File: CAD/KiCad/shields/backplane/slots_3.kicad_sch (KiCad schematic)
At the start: 2 parts

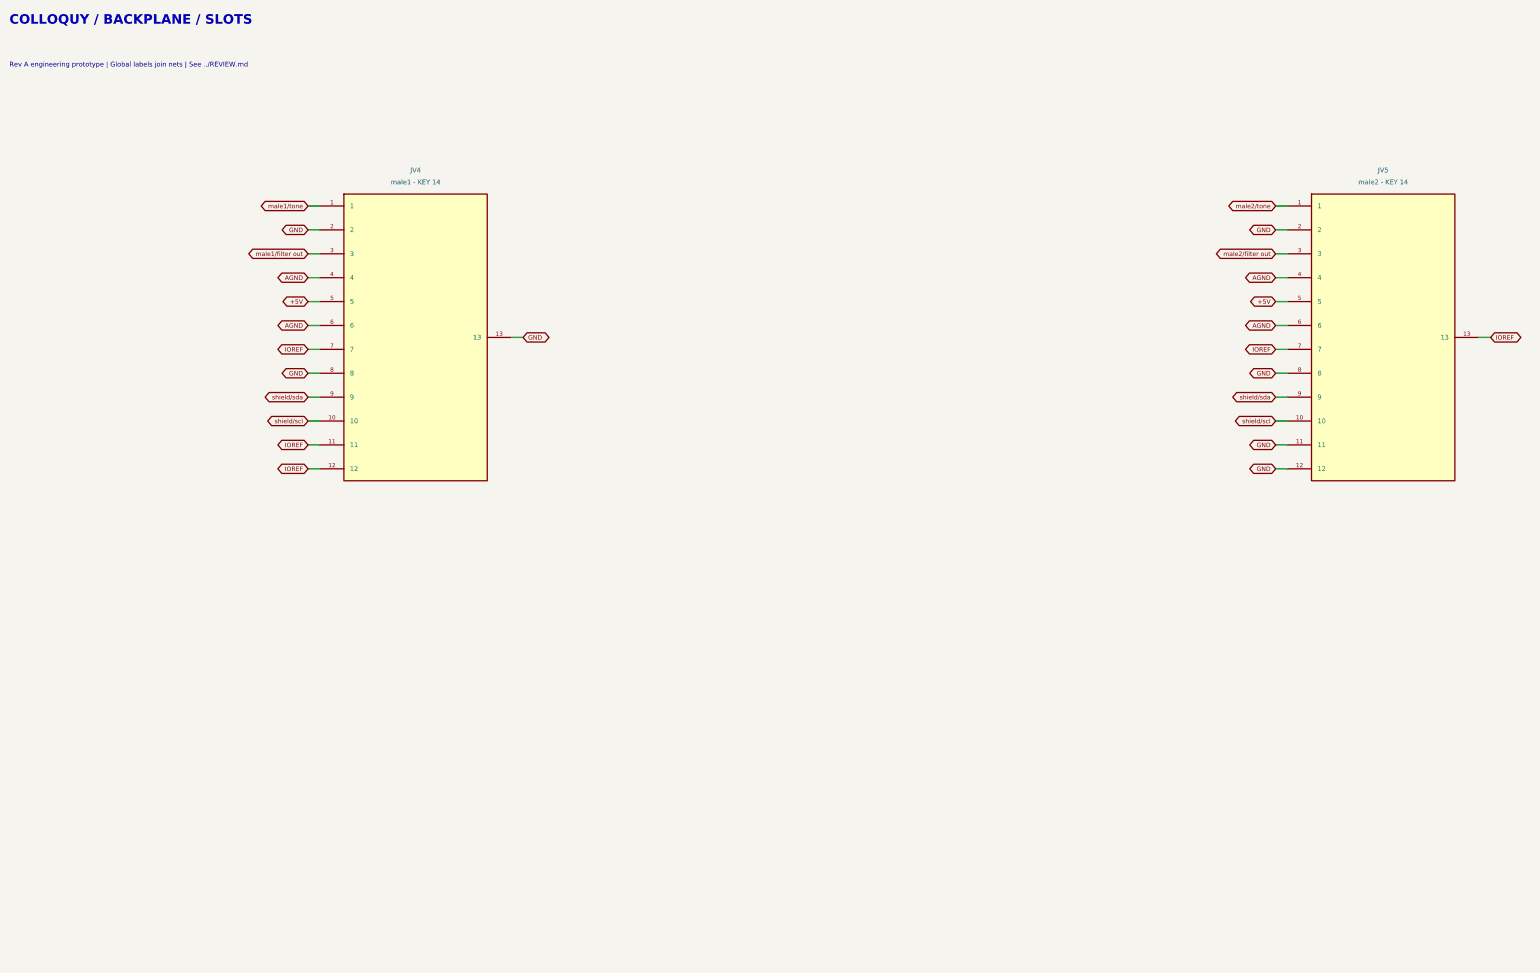
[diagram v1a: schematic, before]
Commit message: Remove shield identification and adopt the simplified connector and Teensy pin maps
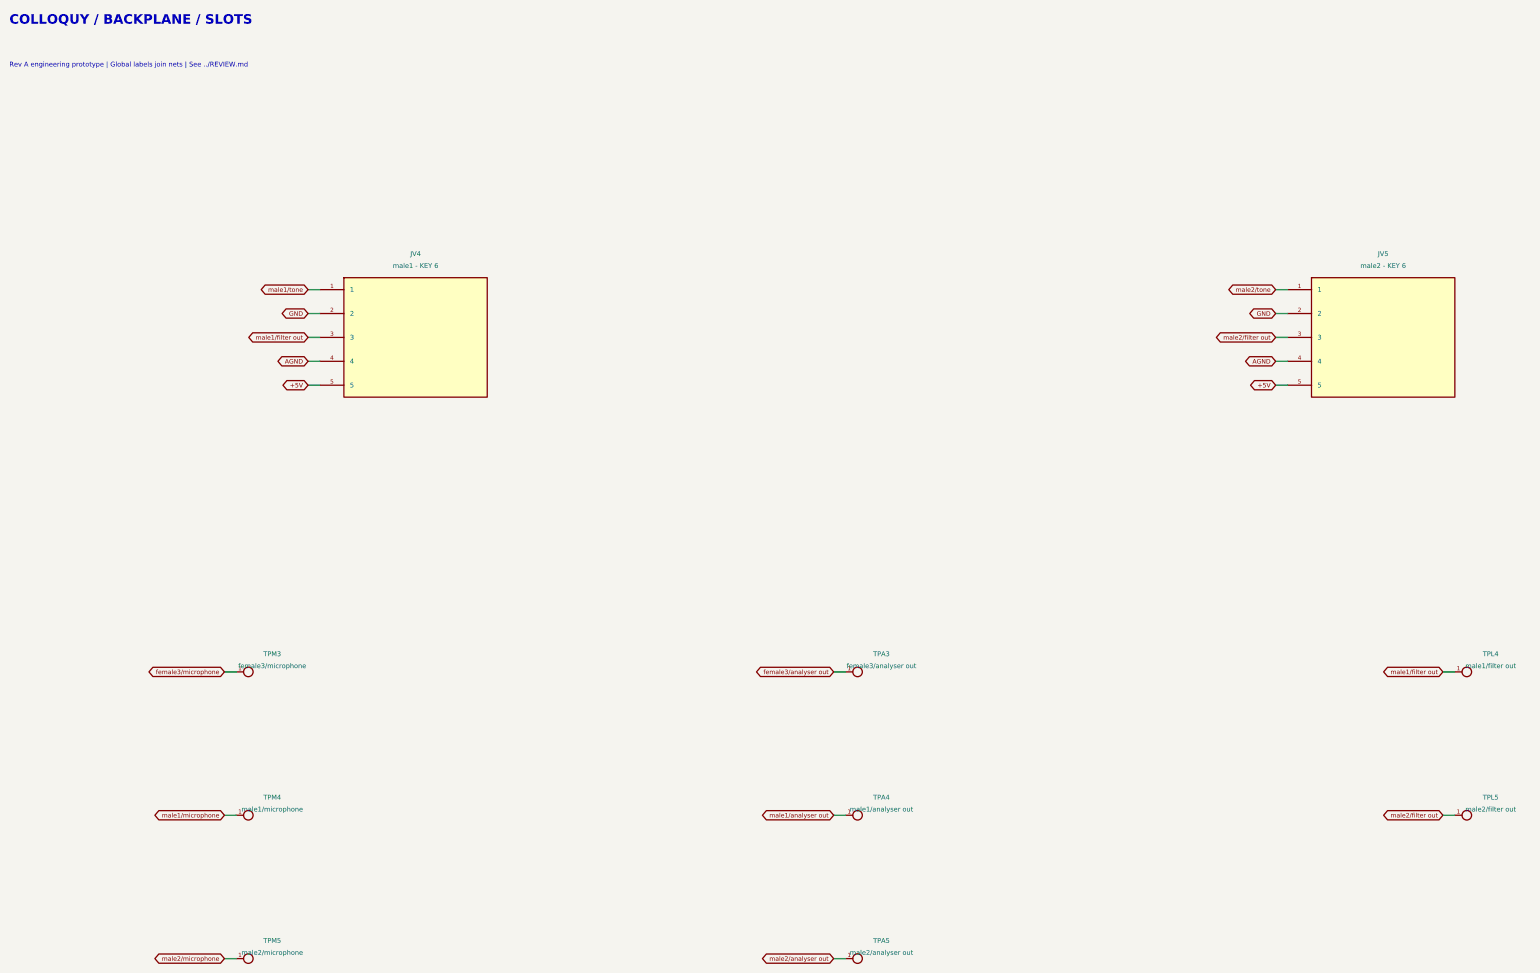
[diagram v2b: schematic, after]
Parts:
- added TPA3: female3/analyser out, Shields:TestPoint_Pad_D1.5mm, symbol Colloquy:TPA3
- added TPA4: male1/analyser out, Shields:TestPoint_Pad_D1.5mm, symbol Colloquy:TPA4
- added TPA5: male2/analyser out, Shields:TestPoint_Pad_D1.5mm, symbol Colloquy:TPA5
- added TPL4: male1/filter out, Shields:TestPoint_Pad_D1.5mm, symbol Colloquy:TPL4
- added TPL5: male2/filter out, Shields:TestPoint_Pad_D1.5mm, symbol Colloquy:TPL5
- added TPM3: female3/microphone, Shields:TestPoint_Pad_D1.5mm, symbol Colloquy:TPM3
- added TPM4: male1/microphone, Shields:TestPoint_Pad_D1.5mm, symbol Colloquy:TPM4
- added TPM5: male2/microphone, Shields:TestPoint_Pad_D1.5mm, symbol Colloquy:TPM5
- JV4: value male1 - KEY 14 -> male1 - KEY 6; footprint Shields:Header_2x07_Key14 -> Shields:Header_2x03_Key6
- JV5: value male2 - KEY 14 -> male2 - KEY 6; footprint Shields:Header_2x07_Key14 -> Shields:Header_2x03_Key6
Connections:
- net AGND: no longer JV4.6, JV5.6
- net GND: no longer JV4.13, JV4.8, JV5.11, JV5.12, JV5.8
- net male1/filter out: now also TPL4.1
- net male2/filter out: now also TPL5.1
- removed net IOREF: JV4.11, JV4.12, JV4.7, JV5.13, JV5.7
- removed net shield/scl: JV4.10, JV5.10
- removed net shield/sda: JV4.9, JV5.9
- new net female3/analyser out: TPA3.1
- new net female3/microphone: TPM3.1
- new net male1/analyser out: TPA4.1
- new net male1/microphone: TPM4.1
- new net male2/analyser out: TPA5.1
- new net male2/microphone: TPM5.1

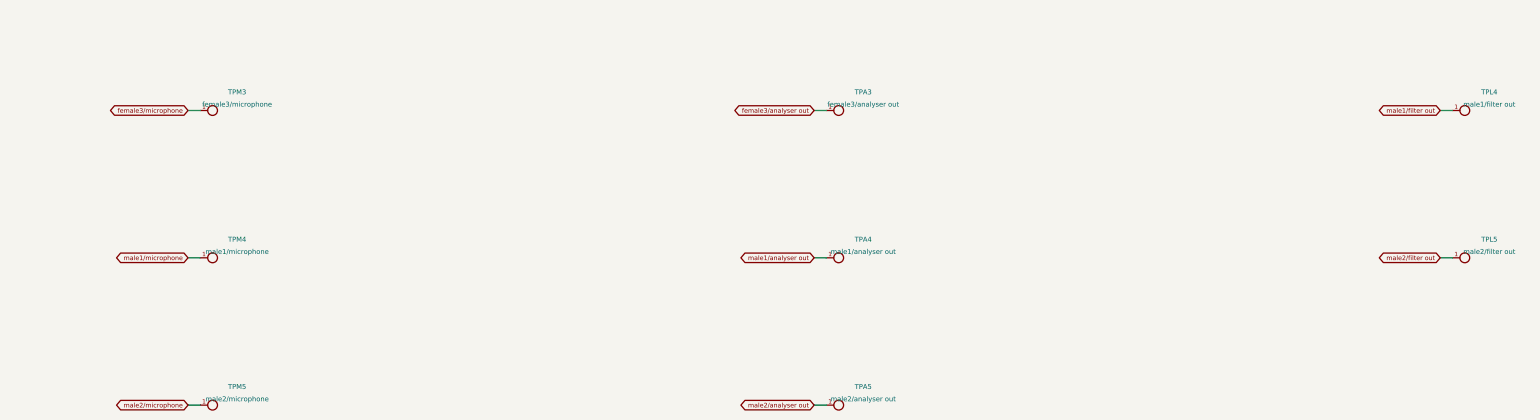
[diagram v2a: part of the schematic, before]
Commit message: Route microphones directly to Teensy and remove the analyser buffer board
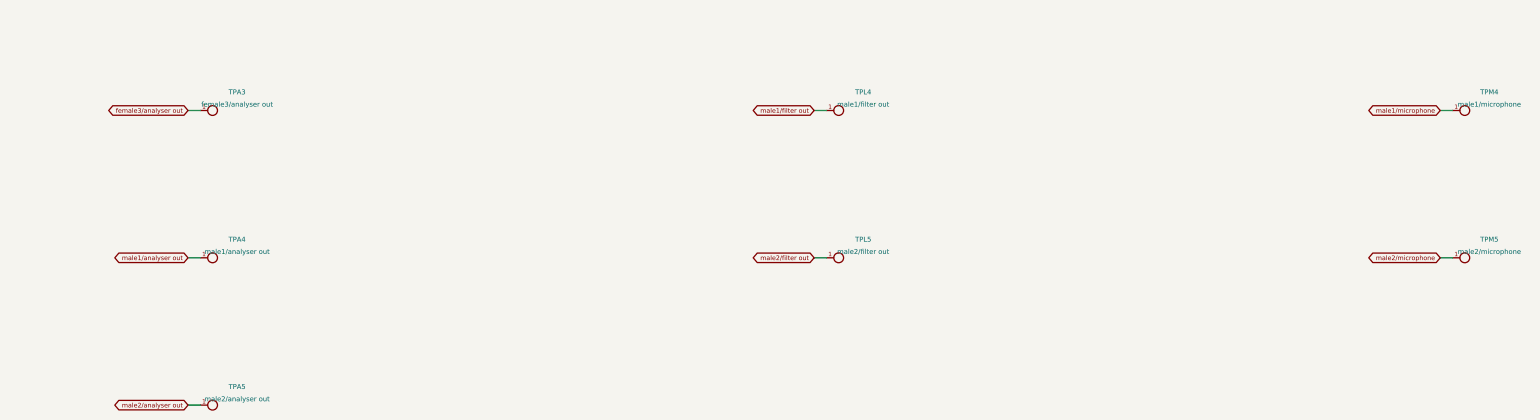
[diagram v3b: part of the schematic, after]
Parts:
- removed TPM3: female3/microphone, Shields:TestPoint_Pad_D1.5mm, symbol Colloquy:TPM3
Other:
- moved on the sheet: TPA3, TPA4, TPA5, TPL4, TPL5, TPM4, TPM5

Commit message: Update shields for Thomas RC cards, debug headers and body microphones
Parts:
- removed TPA3: female3/analyser out, Shields:TestPoint_Pad_D1.5mm, symbol Colloquy:TPA3
- removed TPA4: male1/analyser out, Shields:TestPoint_Pad_D1.5mm, symbol Colloquy:TPA4
- removed TPA5: male2/analyser out, Shields:TestPoint_Pad_D1.5mm, symbol Colloquy:TPA5
- removed TPL4: male1/filter out, Shields:TestPoint_Pad_D1.5mm, symbol Colloquy:TPL4
- removed TPL5: male2/filter out, Shields:TestPoint_Pad_D1.5mm, symbol Colloquy:TPL5
- removed TPM4: male1/microphone, Shields:TestPoint_Pad_D1.5mm, symbol Colloquy:TPM4
- removed TPM5: male2/microphone, Shields:TestPoint_Pad_D1.5mm, symbol Colloquy:TPM5
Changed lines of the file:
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@@
 (wire (pts (xy 287.0200 93.9800) (xy 284.4800 93.9800)) (stroke (width 0) (type default)))
 (global_label "+5V" (shape bidirectional) (at 284.4800 93.9800 180) (effects (font (size 0.95 0.95)) (justify right)) (property "Intersheetrefs" "${INTERSHEET_REFS}" (at 284.4800 93.9800 0) (effects (font (size 1.016 1.016))  (hide yes))))
-(symbol (lib_id "Colloquy:TPA3") (at 66.0400 154.9400 0) (unit 1) (exclude_from_sim no) (in_bom no) (on_board yes) (dnp no)
-(property "Reference" "TPA3" (at 71.1200 151.1300 0) (effects (font (size 1.016 1.016))  ))
-(property "Value" "female3/analyser out" (at 71.1200 153.6700 0) (effects (font (size 1.016 1.016))  ))
-(property "Footprint" "Shields:TestPoint_Pad_D1.5mm" (at 66.0400 154.9400 0) (effects (font (size 1.27 1.27))  (hide yes)))
-(property "Datasheet" "" (at 66.0400 154.9400 0) (effects (font (size 1.27 1.27))  (hide yes)))
-(property "Description" "" (at 66.0400 154.9400 0) (effects (font (size 1.27 1.27))  (hide yes)))
-(pin "1")
-(instances (project "backplane" (path "/c974ff16-a701-53ef-8165-966482bbbbae/41ae4712-1962-5c99-85ef-a0ccc72ad0b9" (reference "TPA3") (unit 1)))))
-(wire (pts (xy 63.5000 154.9400) (xy 60.9600 154.9400)) (stroke (width 0) (type default)))
-(global_label "female3/analyser out" (shape bidirectional) (at 60.9600 154.9400 180) (effects (font (size 0.95 0.95)) (justify right)) (property "Intersheetrefs" "${INTERSHEET_REFS}" (at 60.9600 154.9400 0) (effects (font (size 1.016 1.016))  (hide yes))))
-(symbol (lib_id "Colloquy:TPL4") (at 195.5800 154.9400 0) (unit 1) (exclude_from_sim no) (in_bom no) (on_board yes) (dnp no)
-(property "Reference" "TPL4" (at 200.6600 151.1300 0) (effects (font (size 1.016 1.016))  ))
-(property "Value" "male1/filter out" (at 200.6600 153.6700 0) (effects (font (size 1.016 1.016))  ))
-(property "Footprint" "Shields:TestPoint_Pad_D1.5mm" (at 195.5800 154.9400 0) (effects (font (size 1.27 1.27))  (hide yes)))
-(property "Datasheet" "" (at 195.5800 154.9400 0) (effects (font (size 1.27 1.27))  (hide yes)))
-(property "Description" "" (at 195.5800 154.9400 0) (effects (font (size 1.27 1.27))  (hide yes)))
-(pin "1")
-(instances (project "backplane" (path "/c974ff16-a701-53ef-8165-966482bbbbae/41ae4712-1962-5c99-85ef-a0ccc72ad0b9" (reference "TPL4") (unit 1)))))
-(wire (pts (xy 193.0400 154.9400) (xy 190.5000 154.9400)) (stroke (width 0) (type default)))
-(global_label "male1/filter out" (shape bidirectional) (at 190.5000 154.9400 180) (effects (font (size 0.95 0.95)) (justify right)) (property "Intersheetrefs" "${INTERSHEET_REFS}" (at 190.5000 154.9400 0) (effects (font (size 1.016 1.016))  (hide yes))))
-(symbol (lib_id "Colloquy:TPM4") (at 325.1200 154.9400 0) (unit 1) (exclude_from_sim no) (in_bom no) (on_board yes) (dnp no)
-(property "Reference" "TPM4" (at 330.2000 151.1300 0) (effects (font (size 1.016 1.016))  ))
-(property "Value" "male1/microphone" (at 330.2000 153.6700 0) (effects (font (size 1.016 1.016))  ))
-(property "Footprint" "Shields:TestPoint_Pad_D1.5mm" (at 325.1200 154.9400 0) (effects (font (size 1.27 1.27))  (hide yes)))
-(property "Datasheet" "" (at 325.1200 154.9400 0) (effects (font (size 1.27 1.27))  (hide yes)))
-(property "Description" "" (at 325.1200 154.9400 0) (effects (font (size 1.27 1.27))  (hide yes)))
-(pin "1")
-(instances (project "backplane" (path "/c974ff16-a701-53ef-8165-966482bbbbae/41ae4712-1962-5c99-85ef-a0ccc72ad0b9" (reference "TPM4") (unit 1)))))
-(wire (pts (xy 322.5800 154.9400) (xy 320.0400 154.9400)) (stroke (width 0) (type default)))
-(global_label "male1/microphone" (shape bidirectional) (at 320.0400 154.9400 180) (effects (font (size 0.95 0.95)) (justify right)) (property "Intersheetrefs" "${INTERSHEET_REFS}" (at 320.0400 154.9400 0) (effects (font (size 1.016 1.016))  (hide yes))))
-(symbol (lib_id "Colloquy:TPA4") (at 66.0400 185.4200 0) (unit 1) (exclude_from_sim no) (in_bom no) (on_board yes) (dnp no)
-(property "Reference" "TPA4" (at 71.1200 181.6100 0) (effects (font (size 1.016 1.016))  ))
-(property "Value" "male1/analyser out" (at 71.1200 184.1500 0) (effects (font (size 1.016 1.016))  ))
-(property "Footprint" "Shields:TestPoint_Pad_D1.5mm" (at 66.0400 185.4200 0) (effects (font (size 1.27 1.27))  (hide yes)))
-(property "Datasheet" "" (at 66.0400 185.4200 0) (effects (font (size 1.27 1.27))  (hide yes)))
-(property "Description" "" (at 66.0400 185.4200 0) (effects (font (size 1.27 1.27))  (hide yes)))
-(pin "1")
-(instances (project "backplane" (path "/c974ff16-a701-53ef-8165-966482bbbbae/41ae4712-1962-5c99-85ef-a0ccc72ad0b9" (reference "TPA4") (unit 1)))))
-(wire (pts (xy 63.5000 185.4200) (xy 60.9600 185.4200)) (stroke (width 0) (type default)))
-(global_label "male1/analyser out" (shape bidirectional) (at 60.9600 185.4200 180) (effects (font (size 0.95 0.95)) (justify right)) (property "Intersheetrefs" "${INTERSHEET_REFS}" (at 60.9600 185.4200 0) (effects (font (size 1.016 1.016))  (hide yes))))
-(symbol (lib_id "Colloquy:TPL5") (at 195.5800 185.4200 0) (unit 1) (exclude_from_sim no) (in_bom no) (on_board yes) (dnp no)
-(property "Reference" "TPL5" (at 200.6600 181.6100 0) (effects (font (size 1.016 1.016))  ))
-(property "Value" "male2/filter out" (at 200.6600 184.1500 0) (effects (font (size 1.016 1.016))  ))
-(property "Footprint" "Shields:TestPoint_Pad_D1.5mm" (at 195.5800 185.4200 0) (effects (font (size 1.27 1.27))  (hide yes)))
-(property "Datasheet" "" (at 195.5800 185.4200 0) (effects (font (size 1.27 1.27))  (hide yes)))
-(property "Description" "" (at 195.5800 185.4200 0) (effects (font (size 1.27 1.27))  (hide yes)))
-(pin "1")
-(instances (project "backplane" (path "/c974ff16-a701-53ef-8165-966482bbbbae/41ae4712-1962-5c99-85ef-a0ccc72ad0b9" (reference "TPL5") (unit 1)))))
-(wire (pts (xy 193.0400 185.4200) (xy 190.5000 185.4200)) (stroke (width 0) (type default)))
-(global_label "male2/filter out" (shape bidirectional) (at 190.5000 185.4200 180) (effects (font (size 0.95 0.95)) (justify right)) (property "Intersheetrefs" "${INTERSHEET_REFS}" (at 190.5000 185.4200 0) (effects (font (size 1.016 1.016))  (hide yes))))
-(symbol (lib_id "Colloquy:TPM5") (at 325.1200 185.4200 0) (unit 1) (exclude_from_sim no) (in_bom no) (on_board yes) (dnp no)
-(property "Reference" "TPM5" (at 330.2000 181.6100 0) (effects (font (size 1.016 1.016))  ))
-(property "Value" "male2/microphone" (at 330.2000 184.1500 0) (effects (font (size 1.016 1.016))  ))
-(property "Footprint" "Shields:TestPoint_Pad_D1.5mm" (at 325.1200 185.4200 0) (effects (font (size 1.27 1.27))  (hide yes)))
-(property "Datasheet" "" (at 325.1200 185.4200 0) (effects (font (size 1.27 1.27))  (hide yes)))
-(property "Description" "" (at 325.1200 185.4200 0) (effects (font (size 1.27 1.27))  (hide yes)))
-(pin "1")
-(instances (project "backplane" (path "/c974ff16-a701-53ef-8165-966482bbbbae/41ae4712-1962-5c99-85ef-a0ccc72ad0b9" (reference "TPM5") (unit 1)))))
-(wire (pts (xy 322.5800 185.4200) (xy 320.0400 185.4200)) (stroke (width 0) (type default)))
-(global_label "male2/microphone" (shape bidirectional) (at 320.0400 185.4200 180) (effects (font (size 0.95 0.95)) (justify right)) (property "Intersheetrefs" "${INTERSHEET_REFS}" (at 320.0400 185.4200 0) (effects (font (size 1.016 1.016))  (hide yes))))
-(symbol (lib_id "Colloquy:TPA5") (at 66.0400 215.9000 0) (unit 1) (exclude_from_sim no) (in_bom no) (on_board yes) (dnp no)
-(property "Reference" "TPA5" (at 71.1200 212.0900 0) (effects (font (size 1.016 1.016))  ))
-(property "Value" "male2/analyser out" (at 71.1200 214.6300 0) (effects (font (size 1.016 1.016))  ))
-(property "Footprint" "Shields:TestPoint_Pad_D1.5mm" (at 66.0400 215.9000 0) (effects (font (size 1.27 1.27))  (hide yes)))
-(property "Datasheet" "" (at 66.0400 215.9000 0) (effects (font (size 1.27 1.27))  (hide yes)))
-(property "Description" "" (at 66.0400 215.9000 0) (effects (font (size 1.27 1.27))  (hide yes)))
-(pin "1")
-(instances (project "backplane" (path "/c974ff16-a701-53ef-8165-966482bbbbae/41ae4712-1962-5c99-85ef-a0ccc72ad0b9" (reference "TPA5") (unit 1)))))
-(wire (pts (xy 63.5000 215.9000) (xy 60.9600 215.9000)) (stroke (width 0) (type default)))
-(global_label "male2/analyser out" (shape bidirectional) (at 60.9600 215.9000 180) (effects (font (size 0.95 0.95)) (justify right)) (property "Intersheetrefs" "${INTERSHEET_REFS}" (at 60.9600 215.9000 0) (effects (font (size 1.016 1.016))  (hide yes))))
           (embedded_fonts no))
